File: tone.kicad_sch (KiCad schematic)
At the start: 18 parts, among them Q6 2N3904, SW1 SW_SPDT

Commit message: Actualización de esquemáticos
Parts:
- R22, R23, R24, R25, R26, R27, R28, R29, R30, R4*: footprint (none) -> Resistor_THT:R_Axial_DIN0207_L6.3mm_D2.5mm_P7.62mm_Horizontal
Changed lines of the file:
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@@
 (kicad_sch
-	(version 20231120)
+	(version 20250114)
 	(generator "eeschema")
-	(generator_version "8.0")
+	(generator_version "9.0")
 	(paper "A4")
 	(junction
@@
 			)
 		)
-		(property "Footprint" ""
+		(property "Footprint" "Resistor_THT:R_Axial_DIN0207_L6.3mm_D2.5mm_P7.62mm_Horizontal"
 			(at 96.012 93.98 90)
 			(effects
@@
 			)
 		)
-		(property "Footprint" ""
+		(property "Footprint" "Resistor_THT:R_Axial_DIN0207_L6.3mm_D2.5mm_P7.62mm_Horizontal"
 			(at 106.172 93.98 90)
 			(effects
@@
 			)
 		)
-		(property "Footprint" ""
+		(property "Footprint" "Resistor_THT:R_Axial_DIN0207_L6.3mm_D2.5mm_P7.62mm_Horizontal"
 			(at 96.012 128.27 90)
 			(effects
@@
 			)
 		)
-		(property "Footprint" ""
+		(property "Footprint" "Resistor_THT:R_Axial_DIN0207_L6.3mm_D2.5mm_P7.62mm_Horizontal"
 			(at 118.872 93.98 90)
 			(effects
@@
 			)
 		)
-		(property "Footprint" ""
+		(property "Footprint" "Resistor_THT:R_Axial_DIN0207_L6.3mm_D2.5mm_P7.62mm_Horizontal"
 			(at 184.912 107.95 90)
 			(effects
@@
 			)
 		)
-		(property "Footprint" ""
+		(property "Footprint" "Resistor_THT:R_Axial_DIN0207_L6.3mm_D2.5mm_P7.62mm_Horizontal"
 			(at 172.212 107.95 90)
 			(effects
@@
 			)
 		)
-		(property "Footprint" ""
+		(property "Footprint" "Resistor_THT:R_Axial_DIN0207_L6.3mm_D2.5mm_P7.62mm_Horizontal"
 			(at 184.912 78.74 90)
 			(effects
@@
 			)
 		)
-		(property "Footprint" ""
+		(property "Footprint" "Resistor_THT:R_Axial_DIN0207_L6.3mm_D2.5mm_P7.62mm_Horizontal"
 			(at 172.212 78.74 90)
 			(effects
@@
 			)
 		)
-		(property "Footprint" ""
+		(property "Footprint" "Resistor_THT:R_Axial_DIN0207_L6.3mm_D2.5mm_P7.62mm_Horizontal"
 			(at 205.232 93.98 90)
 			(effects
@@
 			)
 		)
-		(property "Footprint" ""
+		(property "Footprint" "Resistor_THT:R_Axial_DIN0207_L6.3mm_D2.5mm_P7.62mm_Horizontal"
 			(at 80.772 93.98 90)
 			(effects

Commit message: Actualización esquemáticos
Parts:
- renumbered R4* to R104
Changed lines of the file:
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@@
 			)
 		)
-		(property "Description" ""
+		(property "Description" "Power symbol creates a global label with name \"GND\" , ground"
 			(at 186.69 113.03 0)
 			(effects
@@
 			)
 		)
-		(property "Description" ""
+		(property "Description" "Power symbol creates a global label with name \"GND\" , ground"
 			(at 152.4 100.33 0)
 			(effects
@@
 			)
 		)
-		(property "Description" ""
+		(property "Description" "Switch, single pole double throw"
 			(at 140.97 88.9 0)
 			(effects
@@
 			)
 		)
-		(property "Description" ""
+		(property "Description" "Power symbol creates a global label with name \"GND\" , ground"
 			(at 173.99 113.03 0)
 			(effects
@@
 			)
 		)
-		(property "Description" ""
+		(property "Description" "Power symbol creates a global label with name \"GND\" , ground"
 			(at 114.3 111.76 0)
 			(effects
@@
 			)
 		)
-		(property "Description" ""
+		(property "Description" "Power symbol creates a global label with name \"GND\" , ground"
 			(at 207.01 99.06 0)
 			(effects
@@
 			)
 		)
-		(property "Description" ""
+		(property "Description" "Power symbol creates a global label with name \"GND\" , ground"
 			(at 97.79 134.62 0)
 			(effects
@@
 			)
 		)
-		(property "Description" ""
+		(property "Description" "Power symbol creates a global label with name \"VCC\""
 			(at 186.69 72.39 0)
 			(effects
@@
 			)
 		)
-		(property "Description" ""
+		(property "Description" "Power symbol creates a global label with name \"GND\" , ground"
 			(at 82.55 101.6 0)
 			(effects
@@
 			)
 		)
-		(property "Description" ""
+		(property "Description" "0.2A Ic, 40V Vce, Small Signal NPN Transistor, TO-92"
 			(at 184.15 95.25 0)
 			(effects
@@
 			)
 		)
-		(property "Description" ""
+		(property "Description" "Power symbol creates a global label with name \"VCC\""
 			(at 173.99 72.39 0)
 			(effects
@@
 		(dnp no)
 		(fields_autoplaced yes)
-		(property "Reference" "R4*"
-			(at 85.09 92.71 0)
+		(property "Reference" "R104"
+			(at 85.09 92.7099 0)
 			(effects
 				(font
@@
 		)
 		(property "Value" "1M"
-			(at 85.09 95.25 0)
+			(at 85.09 95.2499 0)
 			(effects
 				(font
@@
 			(project "test"
 				(path "/6df9a4de-ce35-4607-9a42-d3c459c15494/9ce8fb74-7855-4494-a29d-3ade1c5b6629"
-					(reference "R4*")
-					(unit 1)
-				)
+					(reference "R104")
+					(unit 1)
+				)

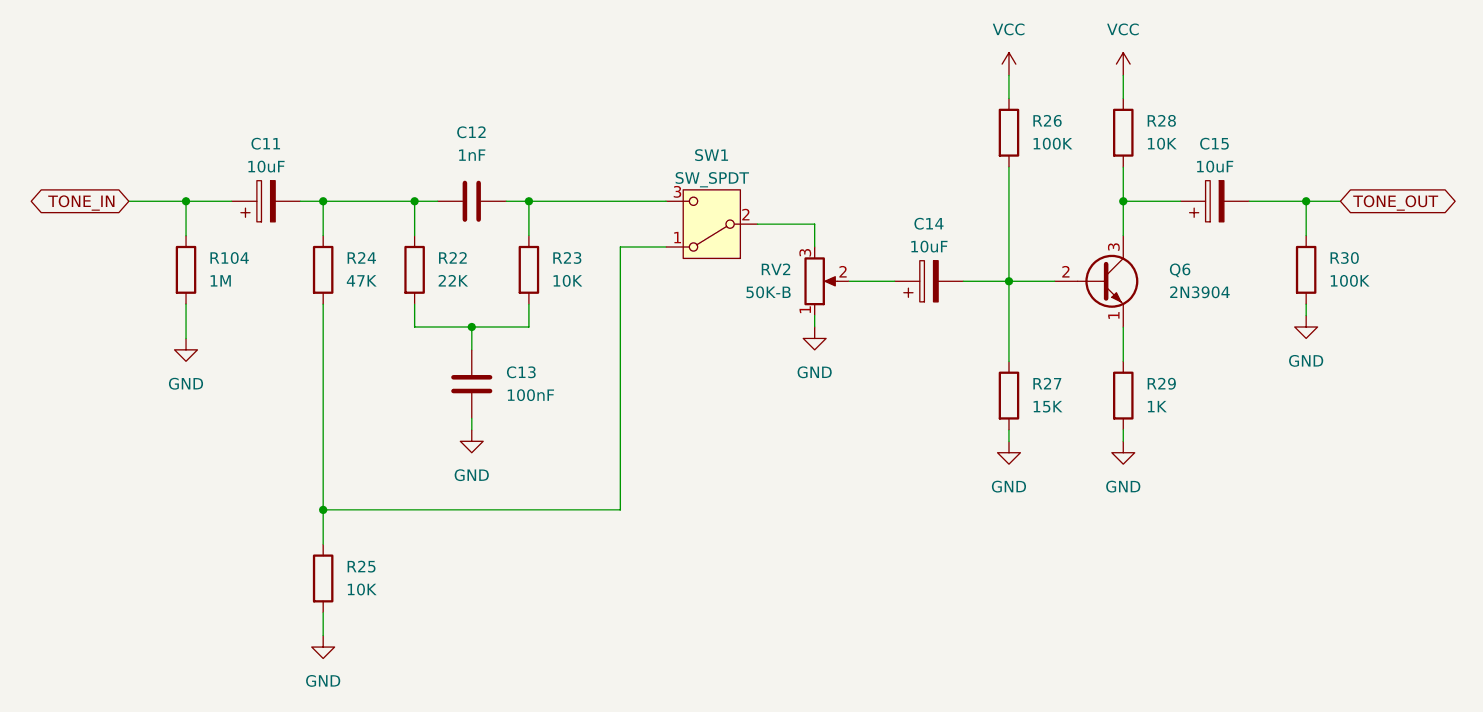
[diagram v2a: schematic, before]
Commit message: Asignación de huellas a componentes.
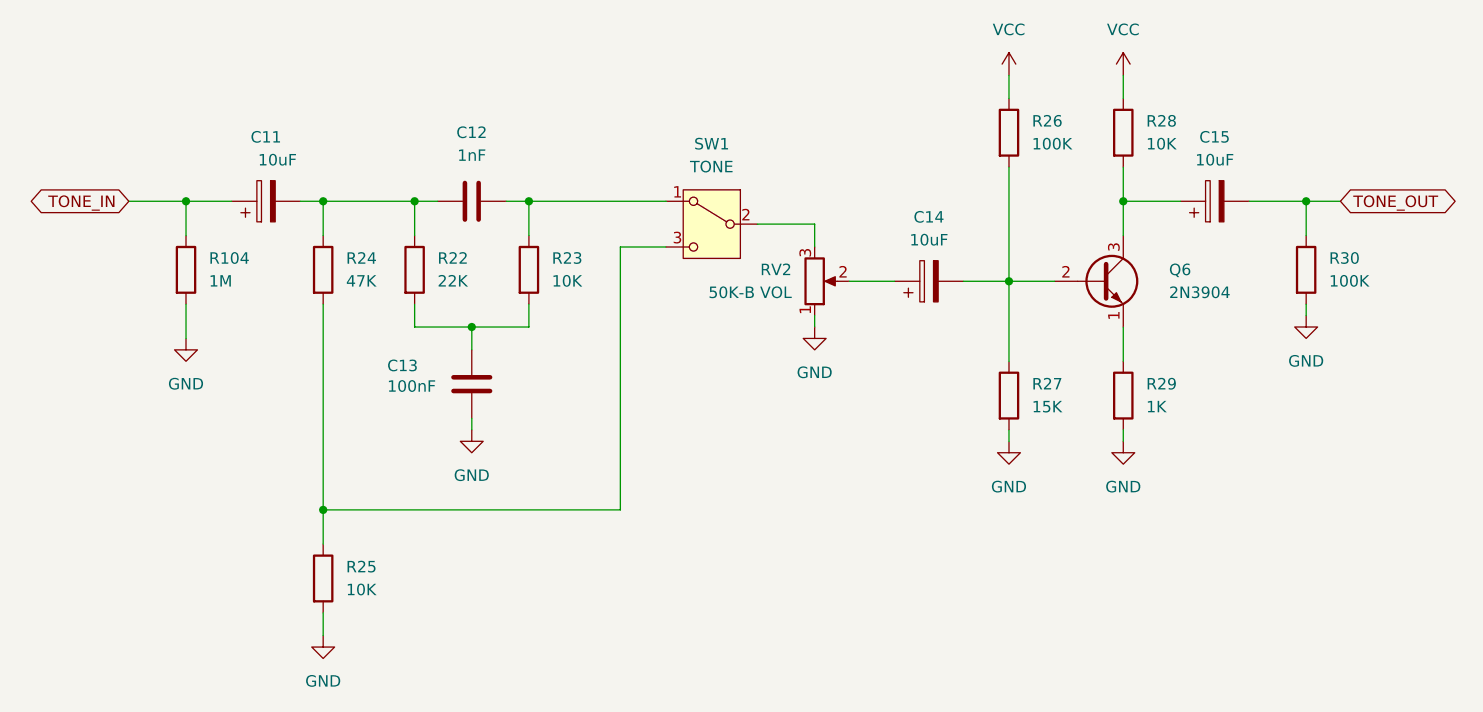
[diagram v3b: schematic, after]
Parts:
- removed SW1: SW_SPDT, symbol Switch:SW_SPDT
- added SW1: TONE, DIY_jorge:SW_DPDT, symbol DIY_jorge:SW_SPDT
- C11, C14, C15: footprint (none) -> Capacitor_THT:CP_Radial_D5.0mm_P2.00mm
- C12, C13: footprint (none) -> Capacitor_THT:C_Disc_D5.1mm_W3.2mm_P5.00mm
- RV2: value 50K-B -> 50K-B VOL; footprint (none) -> DIY_jorge:Pot Alpha 16mm
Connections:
- net at R24.2, R25.1: now also SW1.3
- net at RV2.3: now also SW1.2
- net at C12.2, R23.1: now also SW1.1

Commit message: Adctualización de PCB
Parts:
- removed SW1: TONE, DIY_jorge:SW_DPDT, symbol DIY_jorge:SW_SPDT
- added SW1: TONE, DIY_jorge:SW_SPDT_V2, symbol Switch:SW_Nidec_CAS-120A1
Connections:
- net at R24.2, R25.1: now also SW1.1 (C)
- net at RV2.3: now also SW1.2 (B)
- net at C12.2, R23.1: now also SW1.3 (A)
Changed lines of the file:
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@@
+	)
+	(symbol
+		(lib_id "Switch:SW_Nidec_CAS-120A1")
+		(at 140.97 88.9 0)
+		(mirror y)
+		(unit 1)
+		(exclude_from_sim no)
+		(in_bom yes)
+		(on_board yes)
+		(dnp no)
+		(property "Reference" "SW1"
+			(at 140.97 80.772 0)
+			(effects
+				(font
+					(size 1.27 1.27)
+				)
+			)
+		)
+		(property "Value" "TONE"
+			(at 140.716 82.804 0)
+			(effects
+				(font
+					(size 1.27 1.27)
+				)
+			)
+		)
+		(property "Footprint" "DIY_jorge:SW_SPDT_V2"
+			(at 140.97 99.06 0)
+			(effects
+				(font
+					(size 1.27 1.27)
+				)
+				(hide yes)
+			)
+		)
+		(property "Datasheet" ""
+			(at 140.97 96.52 0)
+			(effects
+				(font
+					(size 1.27 1.27)
+				)
+				(hide yes)
+			)
+		)
+		(property "Description" "Switch, single pole double throw"
+			(at 140.97 88.9 0)
+			(effects
+				(font
+					(size 1.27 1.27)
+				)
+				(hide yes)
+			)
+		)
+		(pin "2"
+		)
+		(pin "3"
+		)
+		(pin "1"
+		)
+		(instances
+			(project ""
+				(path "/6df9a4de-ce35-4607-9a42-d3c459c15494/9ce8fb74-7855-4494-a29d-3ade1c5b6629"
+					(reference "SW1")
+					(unit 1)
+				)
+			)
+		)
 	)
 	(symbol
@@
 					(unit 1)
 				)
-			)
-		)
-	)
-	(symbol
-		(lib_id "DIY_jorge:SW_SPDT")
-		(at 140.97 88.9 0)
-		(mirror y)
-		(unit 1)
-		(exclude_from_sim no)
-		(in_bom yes)
-		(on_board yes)
-		(dnp no)
-		(property "Reference" "SW1"
-			(at 140.97 80.01 0)
-			(effects
-				(font
-					(size 1.27 1.27)
-				)
-			)
-		)
-		(property "Value" "TONE"
-			(at 140.97 82.55 0)
-			(effects
-				(font
-					(size 1.27 1.27)
-				)
-			)
-		)
-		(property "Footprint" "DIY_jorge:SW_DPDT"
-			(at 145.288 99.314 0)
-			(effects
-				(font
-					(size 1.27 1.27)
-				)
-				(hide yes)
-			)
-		)
-		(property "Datasheet" "~"
-			(at 140.97 96.52 0)
-			(effects
-				(font
-					(size 1.27 1.27)
-				)
-				(hide yes)
-			)
-		)
-		(property "Description" "Switch, single pole double throw"
-			(at 138.684 96.774 0)
-			(effects
-				(font
-					(size 1.27 1.27)
-				)
-				(hide yes)
-			)
-		)
-		(pin "2"
-		)
-		(pin "3"
-		)
-		(pin "1"
-		)
-		(instances
-			(project ""
-				(path "/6df9a4de-ce35-4607-9a42-d3c459c15494/9ce8fb74-7855-4494-a29d-3ade1c5b6629"
-					(reference "SW1")
-					(unit 1)
-				)

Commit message: Finalización de PCB (archivos fabricación pendientes)
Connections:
- net at C11.2, C12.1, R22.1: now also R24.2; no longer R24.1
- net at R25.1, SW1.1 (C): now also R24.1; no longer R24.2
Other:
- moved on the sheet: R24
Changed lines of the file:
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@@
 	(symbol
 		(lib_id "Device:R")
-		(at 97.79 93.98 0)
+		(at 97.79 93.98 180)
 		(unit 1)
 		(exclude_from_sim no)
@@
 		(fields_autoplaced yes)
 		(property "Reference" "R24"
-			(at 100.33 92.71 0)
+			(at 100.33 92.7099 0)
 			(effects
 				(font
 					(size 1.27 1.27)
 				)
-				(justify left)
+				(justify right)
 			)
 		)
 		(property "Value" "47K"
-			(at 100.33 95.25 0)
+			(at 100.33 95.2499 0)
 			(effects
 				(font
 					(size 1.27 1.27)
 				)
-				(justify left)
+				(justify right)
 			)
 		)
 		(property "Footprint" "Resistor_THT:R_Axial_DIN0207_L6.3mm_D2.5mm_P7.62mm_Horizontal"
-			(at 96.012 93.98 90)
+			(at 99.568 93.98 90)
 			(effects
 				(font
